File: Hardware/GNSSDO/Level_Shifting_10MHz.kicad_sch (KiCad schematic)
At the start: 39 parts, among them J8 SMA_Edge, SW5 DPDT_Slide_SMD_7.2x3.5mm, U14 74LVC2T45DC, U15 74LVC2T45DC, U17 LMV7219M5

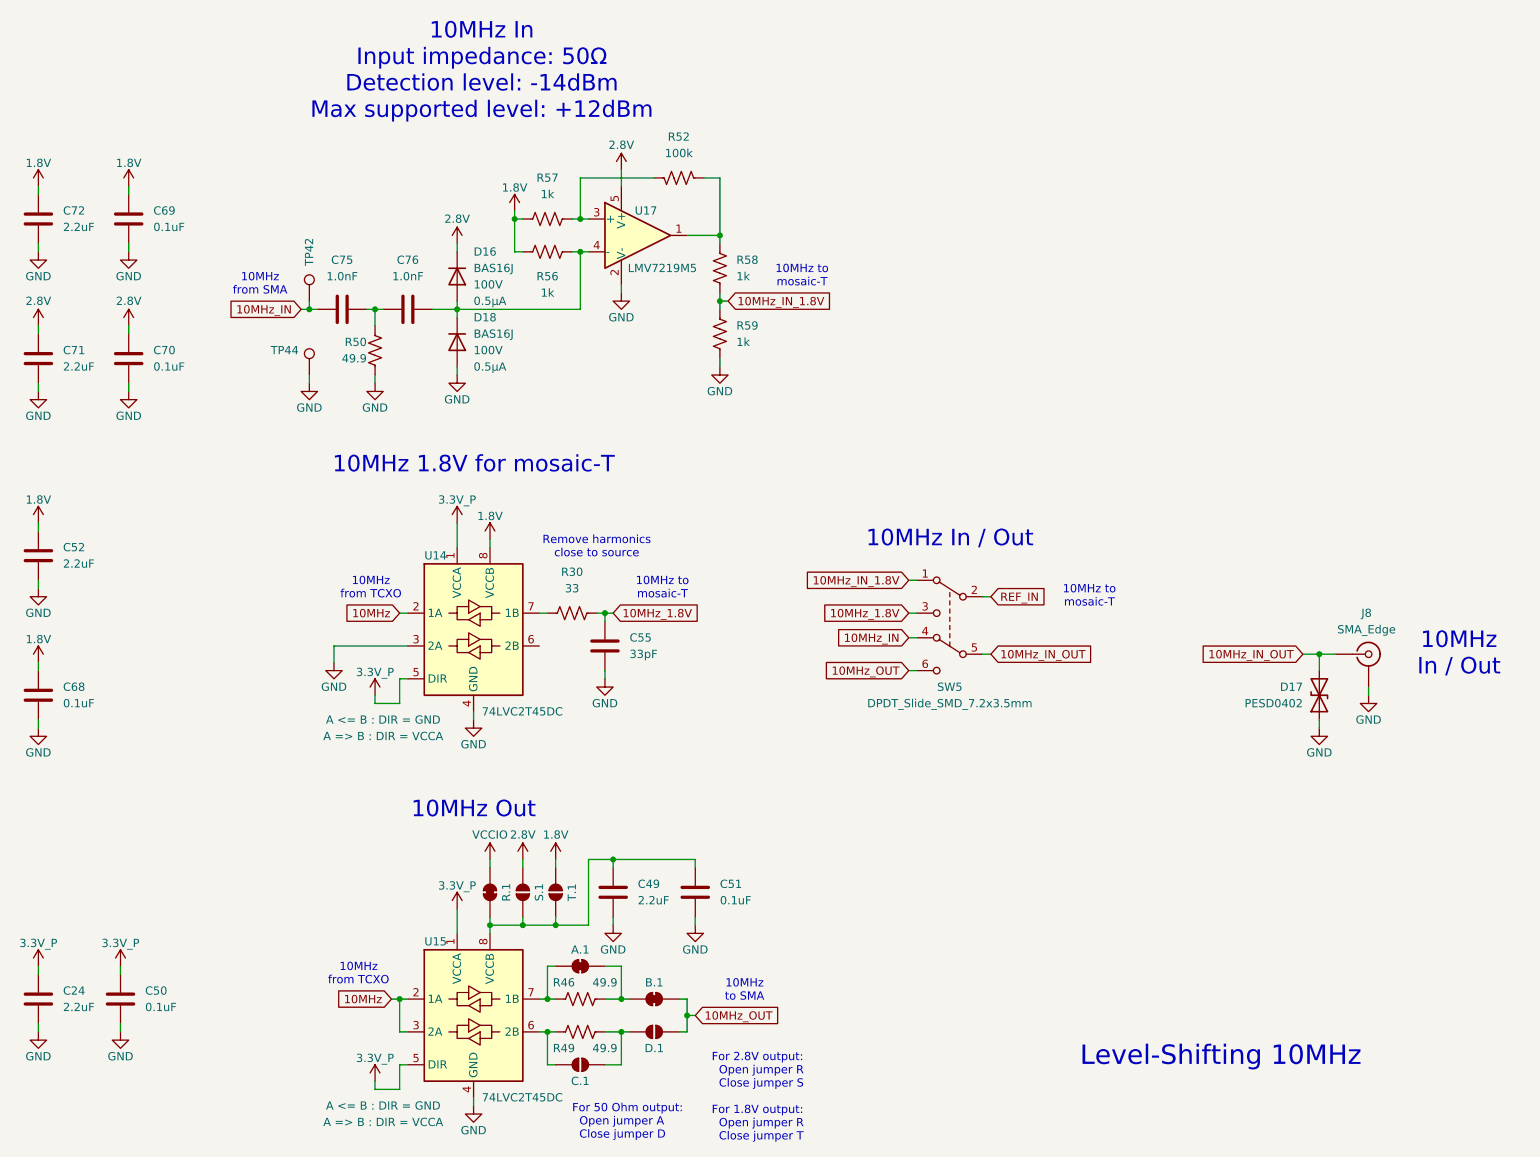
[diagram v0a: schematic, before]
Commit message: KiCad 10
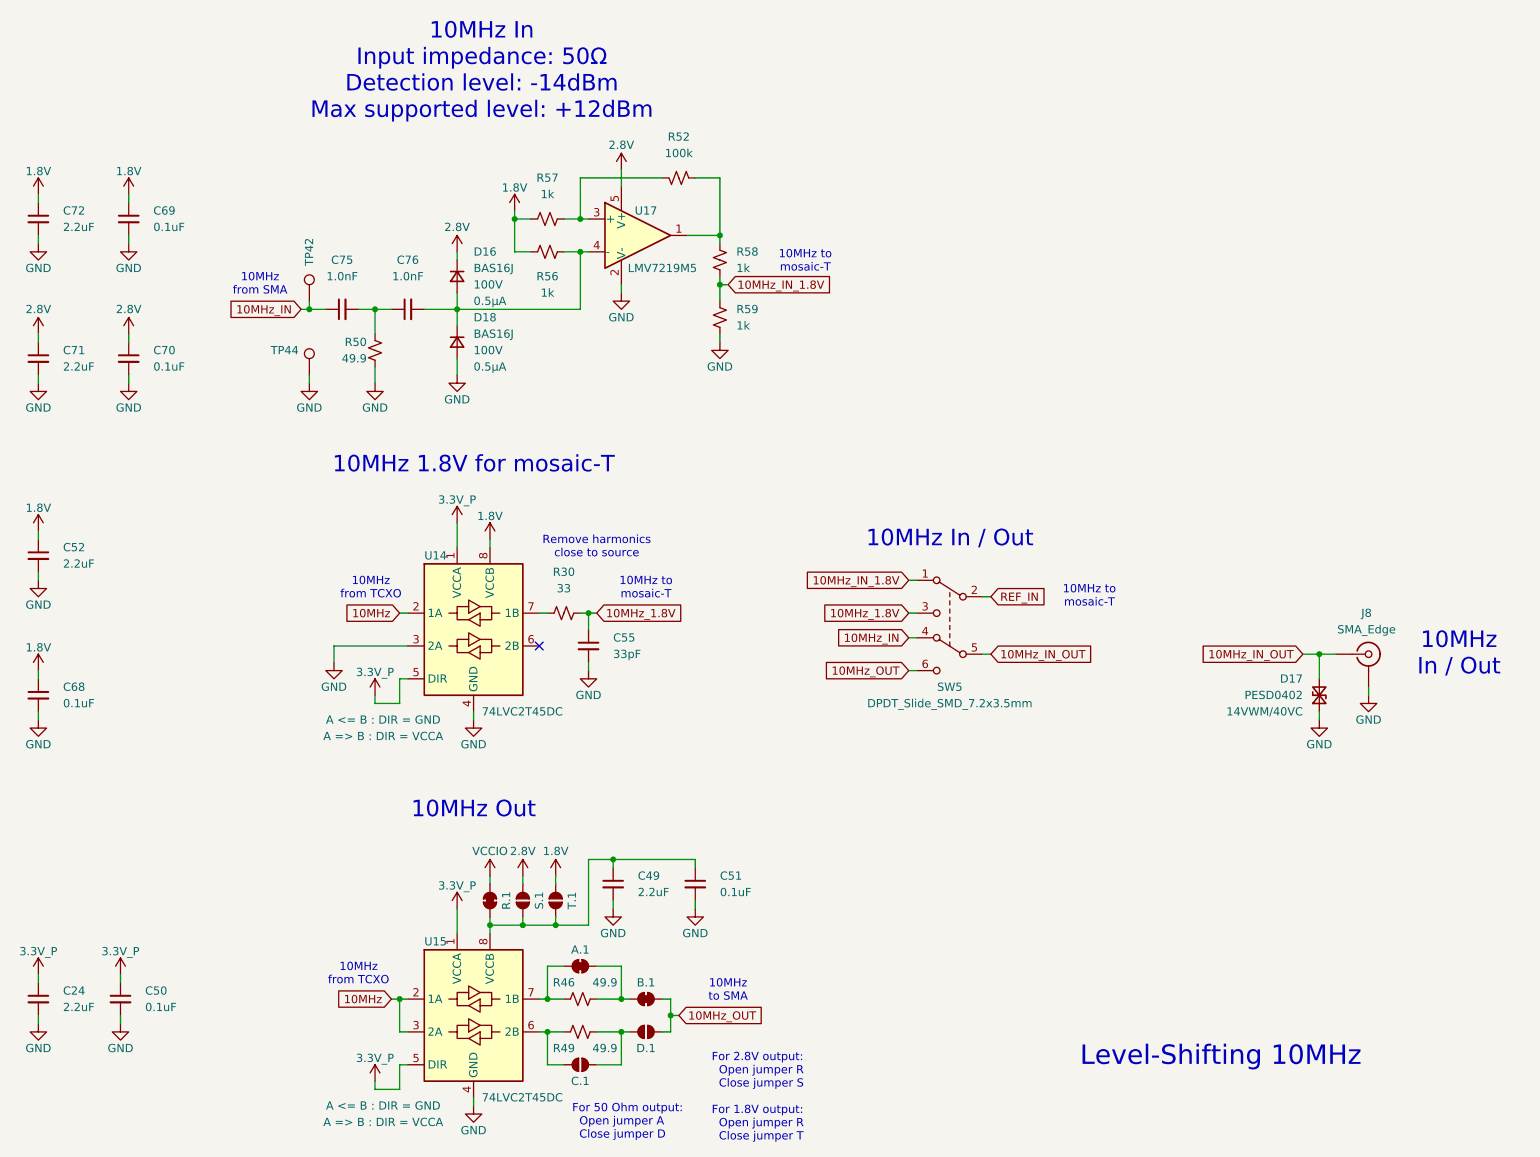
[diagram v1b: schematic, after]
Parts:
- A.1, B.1, C.1, D.1, R.1, S.1, T.1: value ~ -> (none)
- C24, C49, C52, C71, C72: PROD_ID CAP-07888 -> CAP-24999
- D17: symbol SparkFun-DiscreteSemi:D_TVS_0402 -> SparkFun-DiscreteSemi:D_TVS_0402_14V; Rating (none) -> 14VWM/40VC
- J8: footprint SparkFun-Connector:SMA_Edge -> SparkFun-Connector:SMA_Edge_6.3mm; symbol SparkFun-RF:SMA_EdgeMount -> SparkFun-RF:SMA_EdgeMount_6.3mm
- TP42, TP44: footprint SparkFun-Connector:1x01 -> SparkFun-Connector:1x01_P2.54mm
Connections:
- net 1.8V: now also R56.2, R57.2; no longer R56.1, R57.1
- net 10MHz_1.8V: now also R30.2; no longer R30.1
- net 10MHz_IN_1.8V: now also R58.2, R59.1; no longer R58.1, R59.2
- net 2.8V: now also D16.1 (K); no longer D16.C
- net GND: now also D18.2 (A), R50.2, R59.2; no longer D18.A, R50.1, R59.1
- net at A.1.2 (B), B.1.1 (A): now also R46.2; no longer R46.1
- net at C.1.1 (A), U15.6 (2B): now also R49.1; no longer R49.2
- net at C.1.2 (B), D.1.1 (A): now also R49.2; no longer R49.1
- net at A.1.1 (A), U15.7 (1B): now also R46.1; no longer R46.2
- net at U14.7 (1B): now also R30.1; no longer R30.2
- net at C75.2, C76.1: now also R50.1; no longer R50.2
- new net: R52.1, R57.1, U17.3 (+)
- new net: C76.2, D16.2 (A), D18.1 (K), R56.1, U17.4 (-)
- new net: R52.2, R58.1, U17.1
- no-connect marks 0 -> 1
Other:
- moved on the sheet: B.1, C49, C51, C55, D.1, R.1, S.1, T.1
